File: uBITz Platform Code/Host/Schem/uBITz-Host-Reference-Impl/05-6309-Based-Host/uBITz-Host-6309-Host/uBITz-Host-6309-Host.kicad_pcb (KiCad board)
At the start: 4 copper layers, 84.3 x 99.9 mm, 24 parts, among them J3 Conn_01x02_Pin, J4 Conn_02x05_Top_Bottom, U1 MC6809E, U11 24LC16BT-I_SN, U5 ATF1504AS-10AU100, Y1 ACH-14.31818MHZ-EK

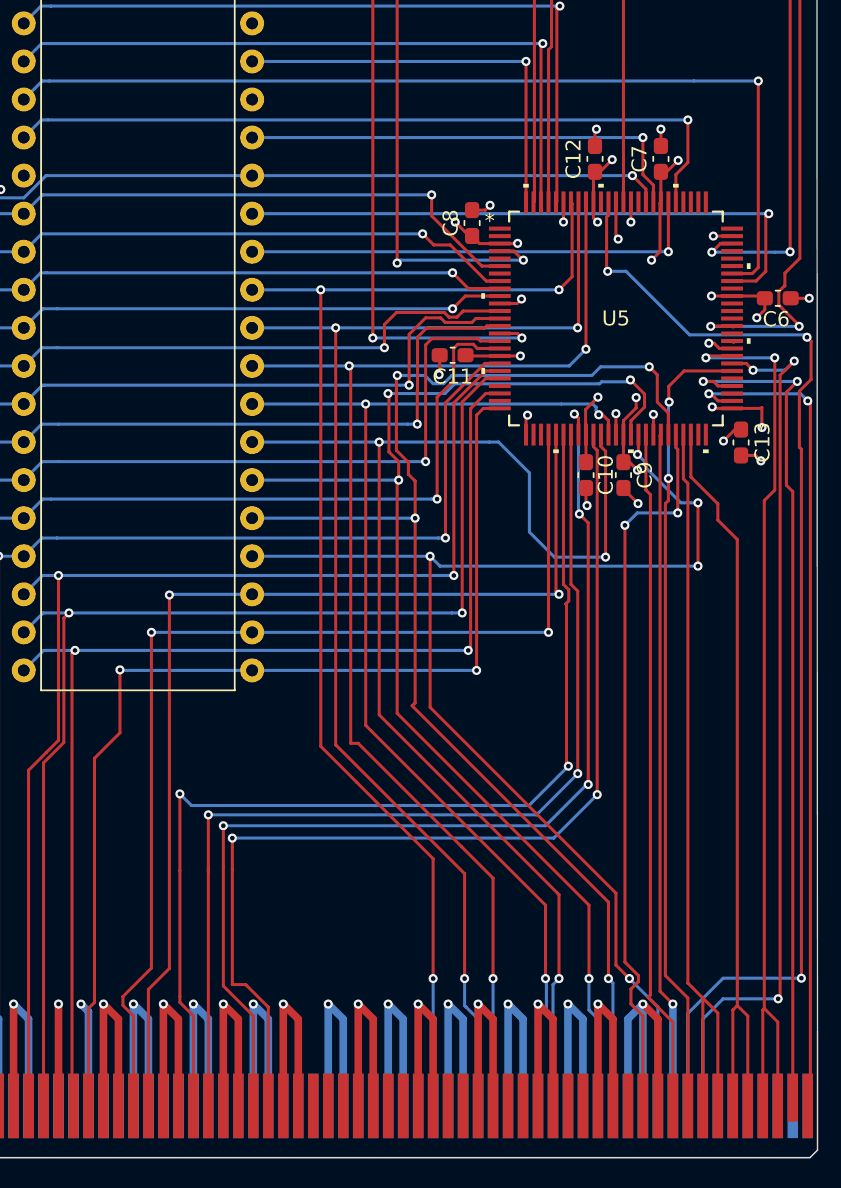
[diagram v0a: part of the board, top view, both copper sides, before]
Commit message: Corrected for bus width (20 -> 19) and allowd mapper to rewrite bits A13-A15 of the address bus (become PA13-PA15)
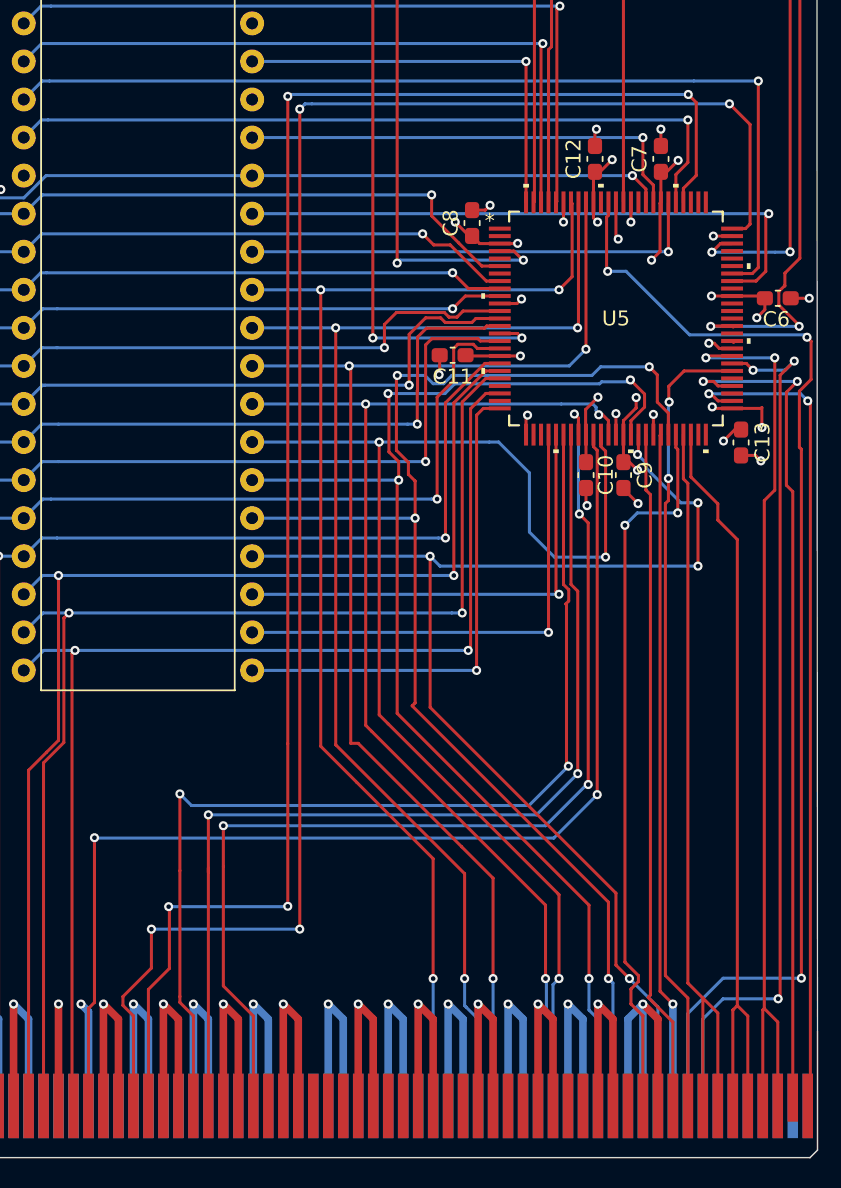
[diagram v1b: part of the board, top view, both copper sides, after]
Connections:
- net /A16 renamed /PA16
- net /A17 renamed /PA17
- net /A18 renamed /PA18
- J1 pad B34: /A13 -> /PA13
- J1 pad B37: /A14 -> /PA14
- J1 pad B38: /A15 -> /PA15
- J1 pad B46: /A19 -> unconnected-(J1A-A19-PadB46)
- U5 pad 35: /A19 -> /PA13
- U5 pad 75: unconnected-(U5-I/O-Pad75) -> /PA14
- U5 pad 79: unconnected-(U5-I/O-Pad79) -> /PA15
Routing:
- net /PA14: track 0.00 -> 116.2 mm, vias 0 -> 4
- net /PA15: track 0.00 -> 110.5 mm, vias 0 -> 4
- net /PA13: track 0.00 -> 77.0 mm, vias 0 -> 2
- net /A19: track 69.1 -> 0.00 mm, vias 2 -> 0
- net /A15: track 71.4 -> 31.2 mm, vias 2 -> 1
- net /A14: track 72.4 -> 33.0 mm, vias 2 -> 1
- net /A13: track 72.6 -> 33.8 mm, vias 2 -> 1

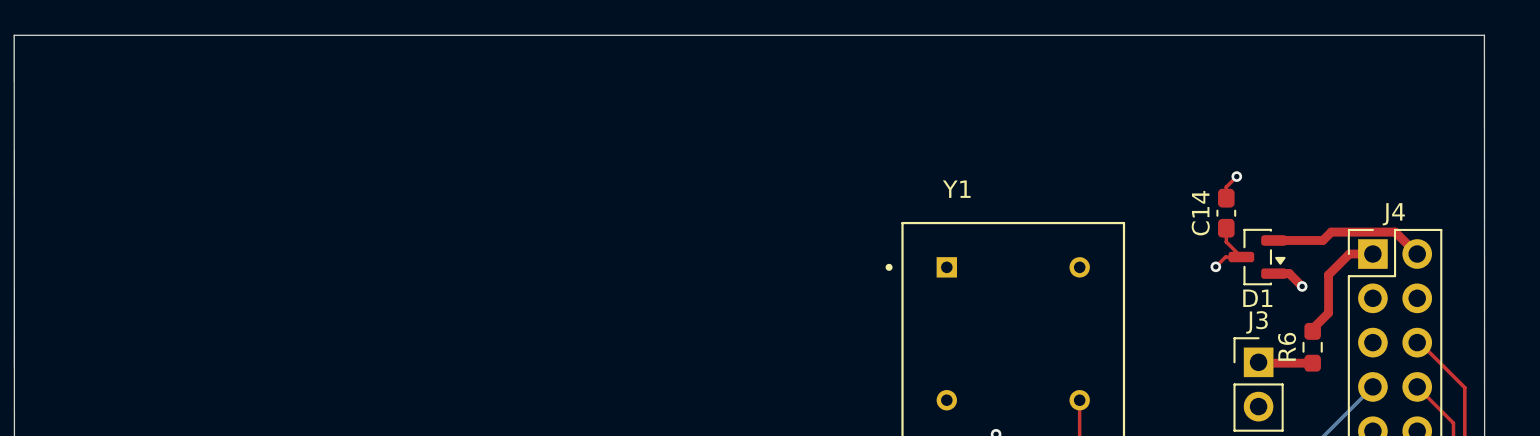
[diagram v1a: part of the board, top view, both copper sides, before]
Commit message: Beautify board and schematic Added PDF
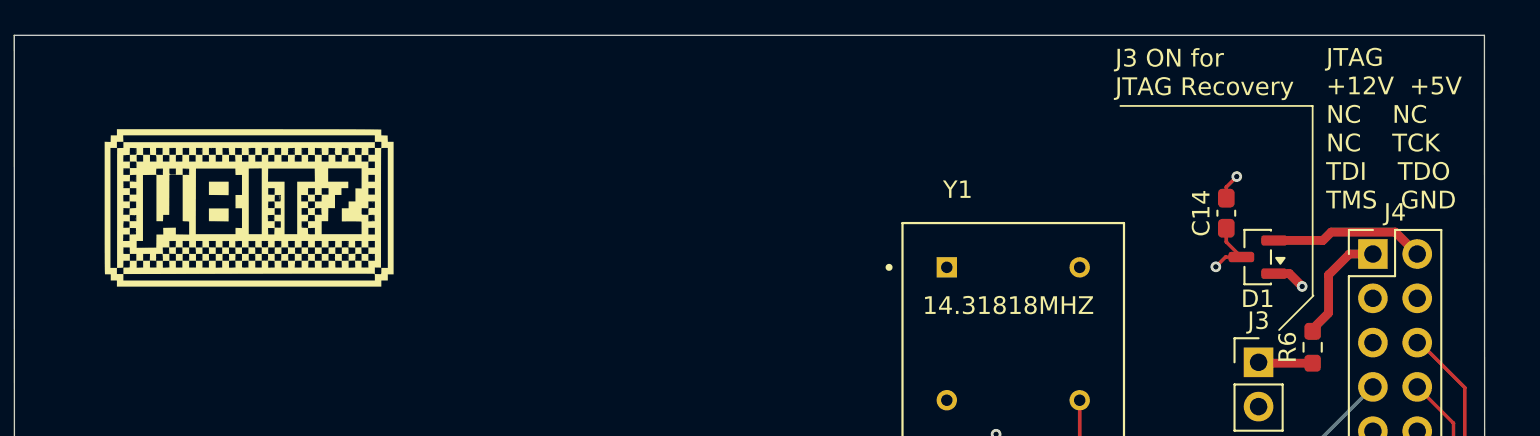
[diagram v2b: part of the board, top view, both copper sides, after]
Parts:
- added G***: LOGO, LOGO, F.Cu at (415.6, 265.3)
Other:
- board text added: "14.31818MHZ"
- board text added: "J3 ON for JTAG Recovery"
- board text added: "JTAG +12V +5V NC NC NC TCK TDI TDO TMS GND"

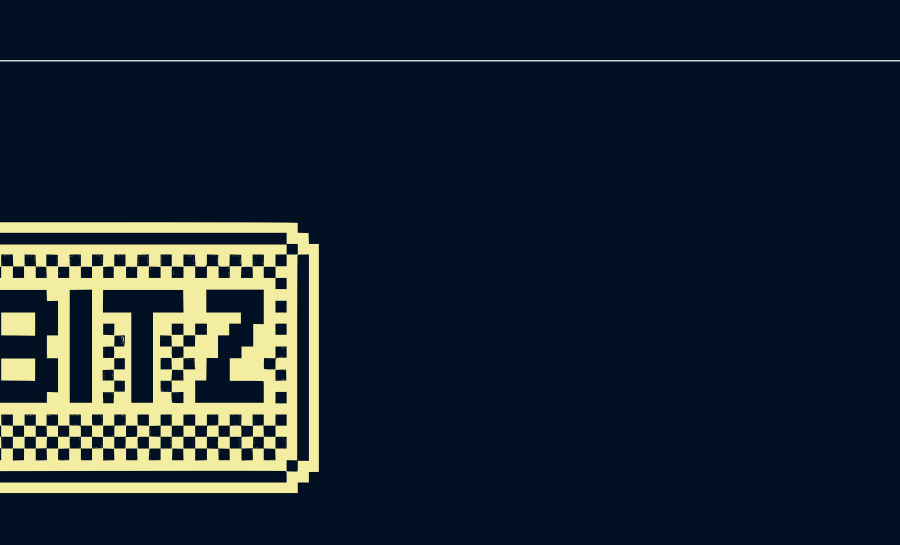
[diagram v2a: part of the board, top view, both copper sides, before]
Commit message: Removed transceivers from Z80 host with the mapper and cleaned up schematics
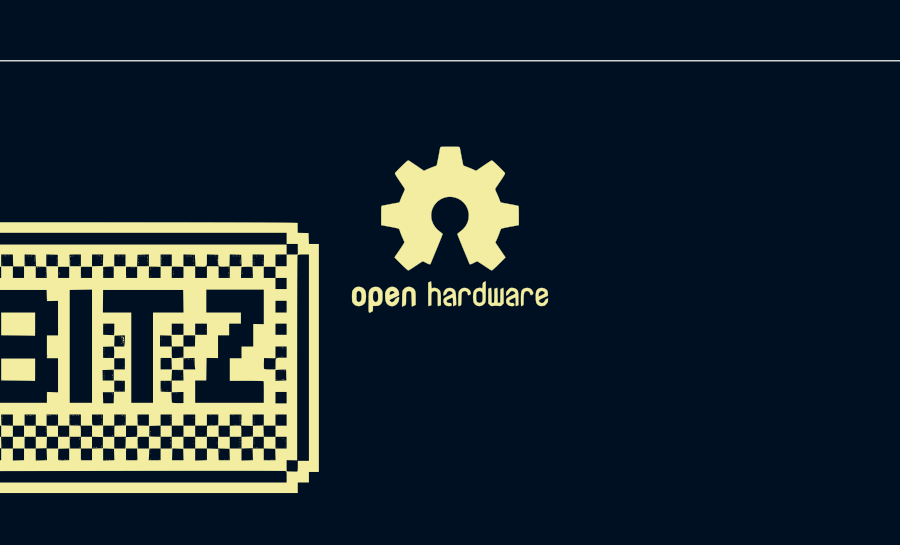
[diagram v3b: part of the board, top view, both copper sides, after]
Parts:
- added REF**: OSHW-Logo2_7.3x6mm_SilkScreen, Symbol:OSHW-Logo2_7.3x6mm_SilkScreen, F.Cu at (428.2, 260.9)
